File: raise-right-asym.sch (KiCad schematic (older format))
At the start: 106 parts, among them IC1 ATTINY88-A, J1 USB_C_Receptacle_16pin, P1 CONN_01X01, P2 CONN_01X01, P3 CONN_01X01, P4 CONN_01X01, P8 CONN_02X03, Q1 PMOS, -3.6A, 0.02R, SW1 kailh hot plug sockets, SW10 kailh hot plug sockets, SW11 kailh hot plug sockets, SW12 kailh hot plug sockets, SW13 kailh hot plug sockets, SW14 kailh hot plug sockets, SW15 kailh hot plug sockets, SW17 kailh hot plug sockets, SW18 kailh hot plug sockets, SW19 kailh hot plug sockets, SW2 kailh hot plug sockets, SW20 kailh hot plug sockets, SW21 kailh hot plug sockets, SW22 kailh hot plug sockets, SW23 kailh hot plug sockets, SW24 kailh hot plug sockets, SW25 kailh hot plug sockets, SW26 kailh hot plug sockets, SW27 kailh hot plug sockets, SW28 kailh hot plug sockets, SW29 kailh hot plug sockets, SW3 kailh hot plug sockets, SW30 kailh hot plug sockets, SW31 kailh hot plug sockets, SW32 kailh hot plug sockets, SW33 kailh hot plug sockets, SW34 kailh hot plug sockets, SW4 kailh hot plug sockets, SW5 kailh hot plug sockets, SW6 kailh hot plug sockets, SW7 kailh hot plug sockets, SW9 kailh hot plug sockets, T1 CONN_01X01, T2 CONN_01X01, T3 CONN_01X01, U1 ss39et

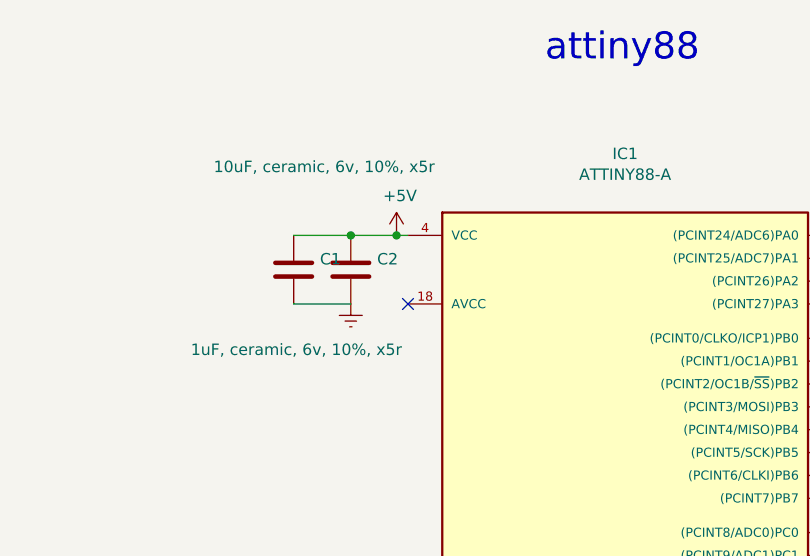
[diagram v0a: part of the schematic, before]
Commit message: avcc to +5v
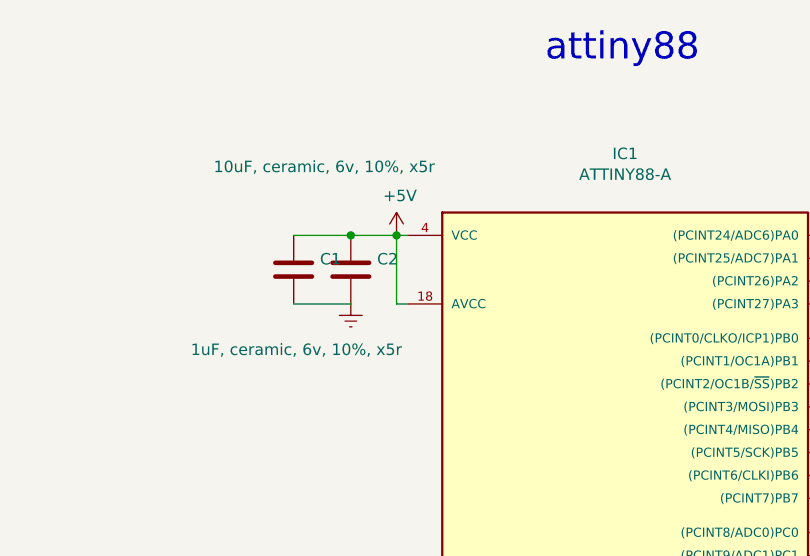
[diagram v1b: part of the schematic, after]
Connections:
- net +5V: now also IC1.18 (AVCC)
- no-connect marks 11 -> 10
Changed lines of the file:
@@
 	1    0    0    -1
 $EndComp
-NoConn ~ 1150 1900
 Text Notes 1750 850  0    118  ~ 0
 attiny88
@@
 	3550 6300 3550 6600
 NoConn ~ -5600 4450
+Wire Wire Line
+	1150 1900 1100 1900
+Wire Wire Line
+	1100 1900 1100 1600
 $EndSCHEMATC

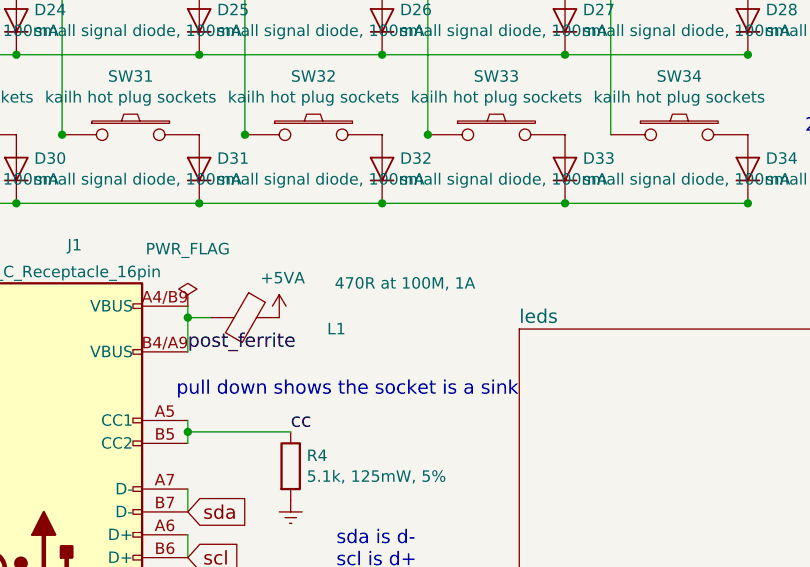
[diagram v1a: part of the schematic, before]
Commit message: add inductor name to component value
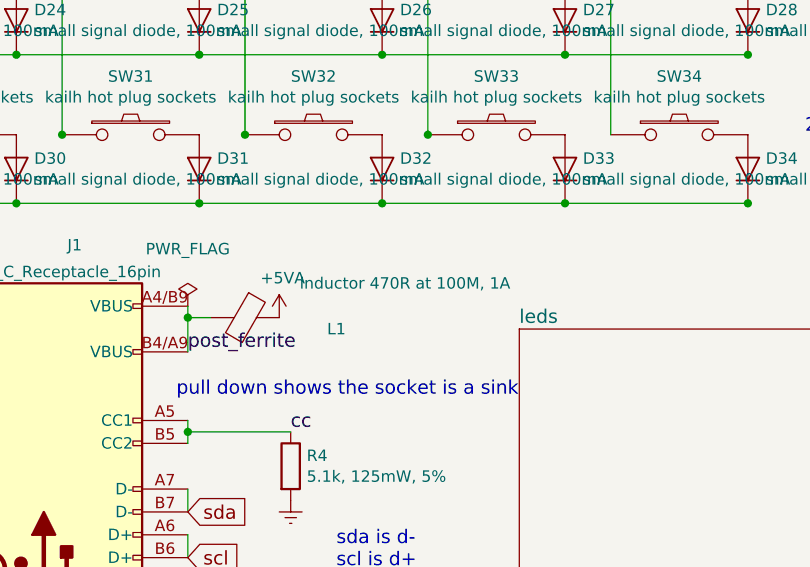
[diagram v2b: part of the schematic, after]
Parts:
- L1: value 470R at 100M, 1A -> inductor 470R at 100M, 1A
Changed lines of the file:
@@
 P 7150 4750
 F 0 "L1" V 7200 5150 50  0000 C CNN
-F 1 "470R at 100M, 1A" V 7000 5450 50  0000 C CNN
+F 1 "inductor 470R at 100M, 1A" V 7000 5450 50  0000 C CNN
 F 2 "raise_fp:R_0603" V 7080 4750 50  0001 C CNN
 F 3 "" H 7150 4750 50  0001 C CNN

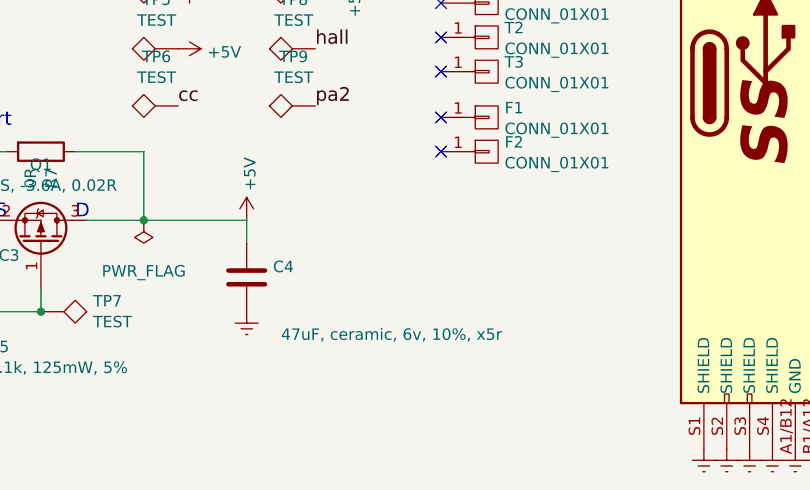
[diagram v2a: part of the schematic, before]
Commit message: changed 47uf ceramic to tantalum
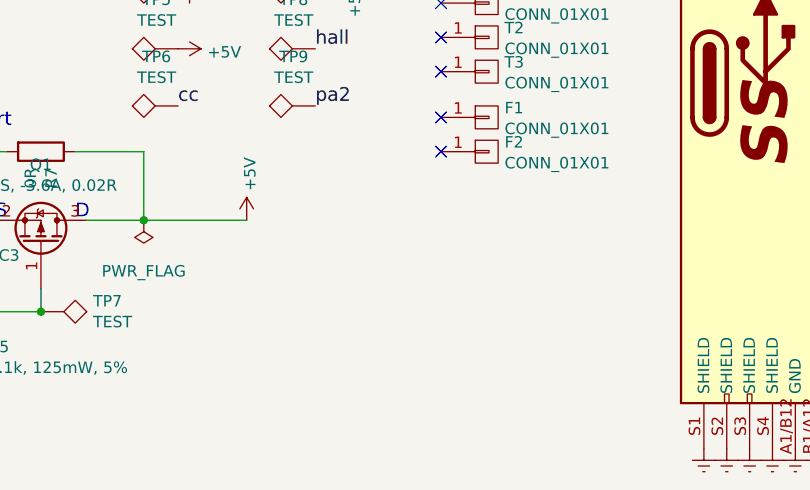
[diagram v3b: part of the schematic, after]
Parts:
- removed C4: 47uF, ceramic, 6v, 10%, x5r, raise_fp:C_1206, symbol C
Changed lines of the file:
@@
 LIBS:test-jig
 LIBS:usb_c_16pin
+LIBS:Device
 EELAYER 26 0
 EELAYER END
@@
 $EndComp
 $Comp
-L Earth #PWR022
-U 1 1 59D15E0F
-P 4000 7000
-F 0 "#PWR022" H 4000 6750 50  0001 C CNN
-F 1 "Earth" H 4000 6850 50  0001 C CNN
-F 2 "" H 4000 7000 50  0000 C CNN
-F 3 "" H 4000 7000 50  0000 C CNN
-	1    4000 7000
-	1    0    0    -1
-$EndComp
-$Comp
 L PWR_FLAG #FLG02
 U 1 1 59D15E15
@@
 firmware pulls addr lines low,\nplace R to make high\nonly place on RHS\n\n
 $Comp
-L C C4
-U 1 1 5ADF91CD
-P 4000 6850
-F 0 "C4" H 4115 6896 50  0000 L CNN
-F 1 "47uF, ceramic, 6v, 10%, x5r" H 4150 6600 50  0000 L CNN
-F 2 "raise_fp:C_1206" H 4038 6700 50  0001 C CNN
-F 3 "" H 4000 6850 50  0000 C CNN
-F 4 "1907522" H 4000 6850 60  0001 C CNN "farnell #"
-F 5 "any/open" H 1200 50  60  0001 C CNN "supplier"
-F 6 "Value" H 4000 6850 60  0001 C CNN "supplier PN"
-F 7 "Value" H 4000 6850 60  0001 C CNN "MOQ"
-F 8 "Value" H 4000 6850 60  0001 C CNN "leadtime"
-	1    4000 6850
-	1    0    0    -1
-$EndComp
-$Comp
 L TEST TP1
 U 1 1 5ADF95BC
@@
 Wire Wire Line
 	3100 7000 2800 7000
-Wire Wire Line
-	4000 6600 4000 6700
 Connection ~ 10150 2400
 Connection ~ 9550 2750

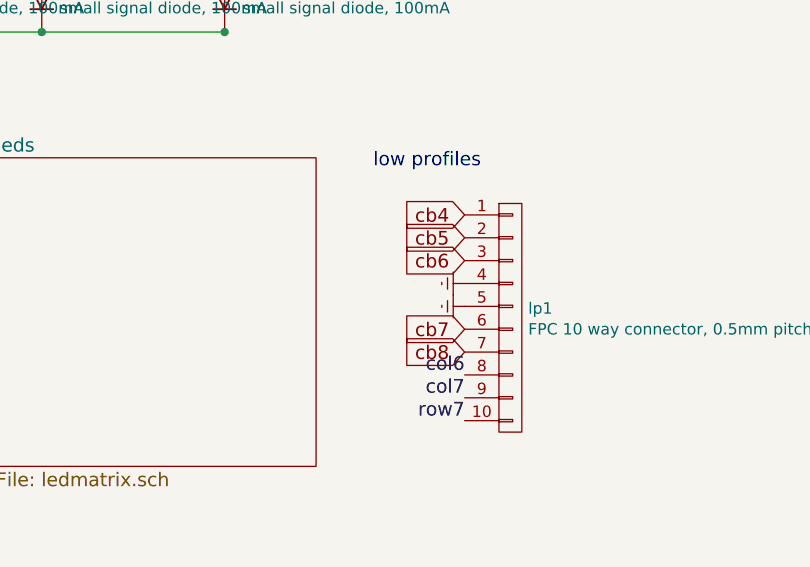
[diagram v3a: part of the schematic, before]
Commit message: new lp led and label name changes to fix ERC
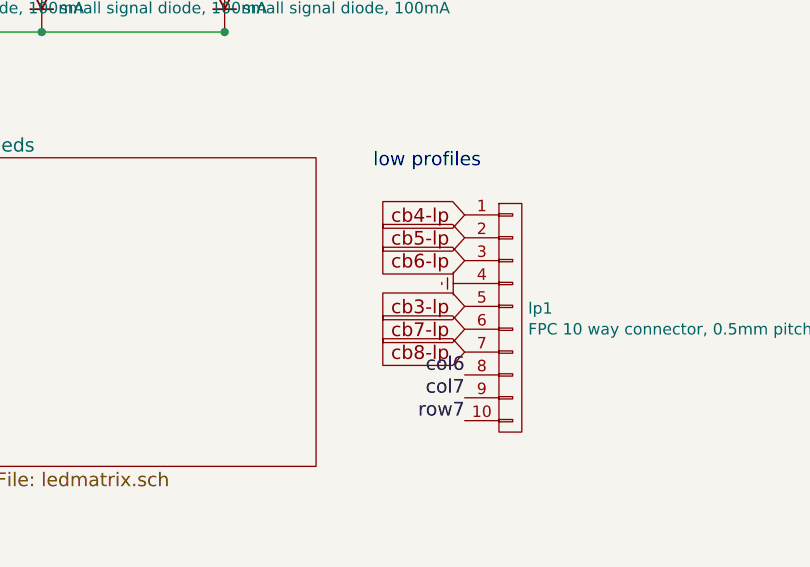
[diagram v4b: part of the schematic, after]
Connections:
- net Earth: no longer lp1.5 (P5)
- net cb4 renamed cb4-lp
- net cb5 renamed cb5-lp
- net cb6 renamed cb6-lp
- net cb7 renamed cb7-lp
- net cb8 renamed cb8-lp
- new net cb3-lp: lp1.5 (P5)
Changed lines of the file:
@@
 low profiles
-$Comp
-L Earth #PWR016
-U 1 1 5ADF52D2
-P 10400 5450
-F 0 "#PWR016" H 10400 5200 50  0001 C CNN
-F 1 "Earth" H 10400 5300 50  0001 C CNN
-F 2 "" H 10400 5450 50  0000 C CNN
-F 3 "" H 10400 5450 50  0000 C CNN
-	1    10400 5450
-	0    1    1    0
-$EndComp
 $Comp
 L Earth #PWR014
@@
 $EndComp
 Text GLabel 10400 5650 0    60   Input ~ 0
-cb8
+cb8-lp
 Text GLabel 10400 5550 0    60   Input ~ 0
-cb7
+cb7-lp
 Text GLabel 10400 5250 0    60   Input ~ 0
-cb6
+cb6-lp
 Text GLabel 10400 5150 0    60   Input ~ 0
-cb5
+cb5-lp
 Text GLabel 10400 5050 0    60   Input ~ 0
-cb4
+cb4-lp
 Text Label 10400 5950 2    60   ~ 0
 row7
@@
 Wire Wire Line
 	1100 1900 1100 1600
+Text GLabel 10400 5450 0    60   Input ~ 0
+cb3-lp
 $EndSCHEMATC

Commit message: changed to 2.2mm mount holes
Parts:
- P1, P2, P3, P4: footprint raise_fp:MountingHole_2.7mm_Pad -> raise_fp:MountingHole_2.2mm_Pad
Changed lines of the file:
@@
 F 0 "P1" H 5128 4991 50  0000 L CNN
 F 1 "CONN_01X01" H 5128 4900 50  0000 L CNN
-F 2 "raise_fp:MountingHole_2.7mm_Pad" H 5050 4950 50  0001 C CNN
+F 2 "raise_fp:MountingHole_2.2mm_Pad" H 5050 4950 50  0001 C CNN
 F 3 "" H 5050 4950 50  0000 C CNN
 F 4 "dnp" H 5050 4950 60  0001 C CNN "farnell #"
@@
 F 0 "P2" H 5128 5141 50  0000 L CNN
 F 1 "CONN_01X01" H 5128 5050 50  0000 L CNN
-F 2 "raise_fp:MountingHole_2.7mm_Pad" H 5050 5100 50  0001 C CNN
+F 2 "raise_fp:MountingHole_2.2mm_Pad" H 5050 5100 50  0001 C CNN
 F 3 "" H 5050 5100 50  0000 C CNN
 F 4 "dnp" H 5050 5100 60  0001 C CNN "farnell #"
@@
 F 0 "P3" H 5128 5291 50  0000 L CNN
 F 1 "CONN_01X01" H 5128 5200 50  0000 L CNN
-F 2 "raise_fp:MountingHole_2.7mm_Pad" H 5050 5250 50  0001 C CNN
+F 2 "raise_fp:MountingHole_2.2mm_Pad" H 5050 5250 50  0001 C CNN
 F 3 "" H 5050 5250 50  0000 C CNN
 F 4 "dnp" H 5050 5250 60  0001 C CNN "farnell #"
@@
 F 0 "P4" H 5128 5441 50  0000 L CNN
 F 1 "CONN_01X01" H 5128 5350 50  0000 L CNN
-F 2 "raise_fp:MountingHole_2.7mm_Pad" H 5050 5400 50  0001 C CNN
+F 2 "raise_fp:MountingHole_2.2mm_Pad" H 5050 5400 50  0001 C CNN
 F 3 "" H 5050 5400 50  0000 C CNN
 F 4 "dnp" H 5050 5400 60  0001 C CNN "farnell #"
